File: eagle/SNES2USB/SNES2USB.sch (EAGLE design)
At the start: 46 parts, among them J1 AVR_SPI_PRG_6PTH, Y1 12-20MHz

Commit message: beta of the SNES2USB PCB
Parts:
- removed JP1, JP2: M021X02_NO_SILK, SparkFun-Connectors:M021X02_NO_SILK
- removed JP3, JP4: M161X16_NO_SILK, SparkFun-Connectors:M161X16_NO_SILK
- removed JP_ID: TEST-POINT3X5, SparkFun-Passives:TEST-POINT3X5
- removed PORTB328: (no value), SparkFun-Connectors:M081X08
- removed RAIL+, RAIL-: M17NOSILK, SparkFun-Connectors:M17NOSILK
- removed U$2, U$3, U$4, U$5, U$6: M191X19_NO_SILK, SparkFun-Connectors:M191X19_NO_SILK
- added J10, J7, J8, J9: (no value), SparkFun-Connectors:CONN_041X04_NO_SILK
- added J2, J3, J4, J5, J6: (no value), SparkFun-Connectors:CONN_08NO_SILK_FEMALE_PTH
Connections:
- removed net B0: PORTB328.1, UC2.PB0(ICP), UC328DIP.PB0(ICP)
- removed net B1: PORTB328.2, UC2.PB1(OC1A), UC328DIP.PB1(OC1A)
- removed net B2: PORTB328.3, UC2.PB2(SS/OC1B), UC328DIP.PB2(SS/OC1B)
- net B6: no longer PORTB328.7
- net B7: no longer PORTB328.8
- net GND: no longer JP2.1, JP2.2, RAIL-.1, RAIL-.10, RAIL-.11, RAIL-.12, RAIL-.13, RAIL-.14, RAIL-.15, RAIL-.16, RAIL-.17, RAIL-.2, RAIL-.3, RAIL-.4, RAIL-.5, RAIL-.6, RAIL-.7, RAIL-.8, RAIL-.9
- net MISO: no longer PORTB328.5
- net MOSI: no longer PORTB328.4
- net N$1: no longer JP_ID.1
- net SCK: no longer PORTB328.6
- net VCC: no longer JP1.1, JP1.2, RAIL+.1, RAIL+.10, RAIL+.11, RAIL+.12, RAIL+.13, RAIL+.14, RAIL+.15, RAIL+.16, RAIL+.17, RAIL+.2, RAIL+.3, RAIL+.4, RAIL+.5, RAIL+.6, RAIL+.7, RAIL+.8, RAIL+.9

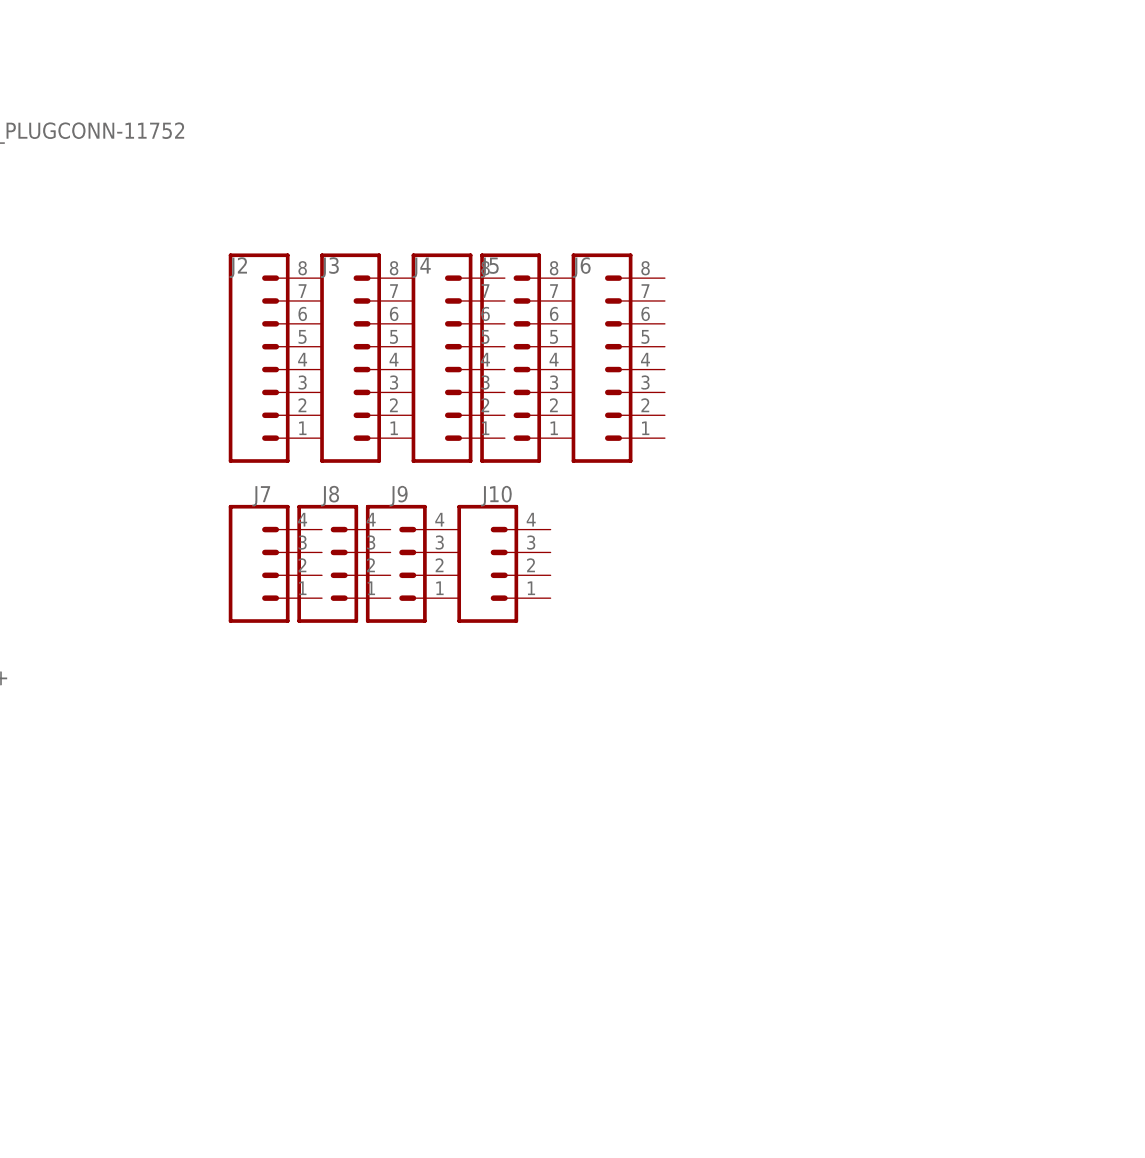
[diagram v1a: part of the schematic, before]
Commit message: SNES2USB nearly ready to be released, todo change for alternate layout of SNES pad
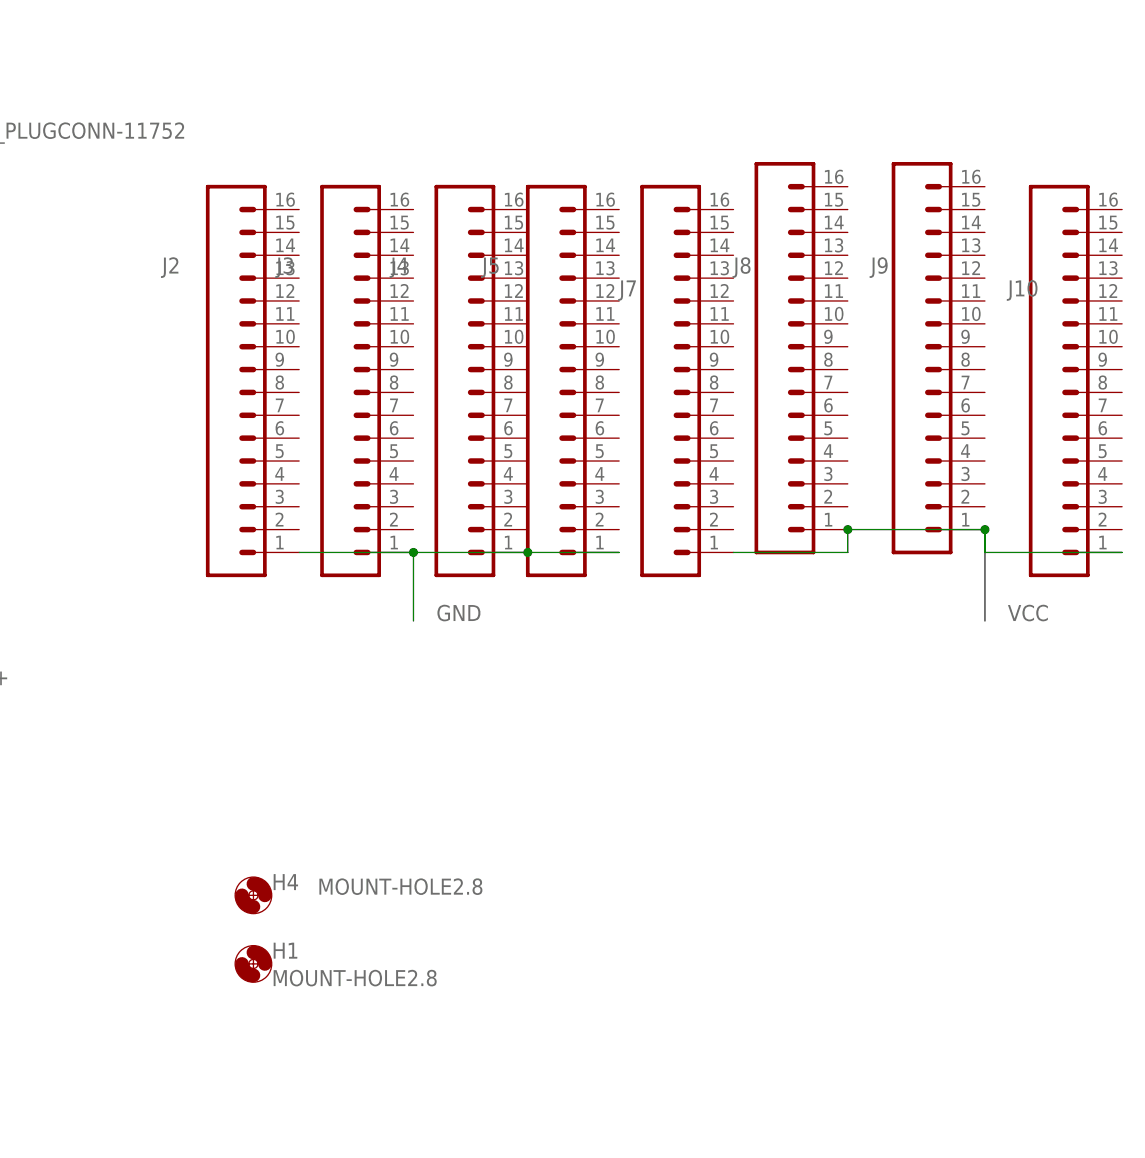
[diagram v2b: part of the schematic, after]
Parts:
- removed J6: (no value), SparkFun-Connectors:CONN_08NO_SILK_FEMALE_PTH
- added H1, H4: MOUNT-HOLE2.8, holes:MOUNT-HOLE2.8
- J10, J7, J8, J9: device SparkFun-Connectors:CONN_041X04_NO_SILK -> SparkFun-Connectors:CONN_161X16_NO_SILK
- J2, J3, J4, J5: device SparkFun-Connectors:CONN_08NO_SILK_FEMALE_PTH -> SparkFun-Connectors:CONN_161X16_NO_SILK
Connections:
- net GND: now also J2.1, J3.1, J4.1, J5.1
- net VCC: now also J10.1, J7.1, J8.1, J9.1
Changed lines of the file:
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@@
 <part name="JLATCH" library="SparkFun-Connectors" library_urn="urn:adsk.eagle:library:513" deviceset="CONN_01" device="PTH_NO_SILK_YES_STOP" package3d_urn="urn:adsk.eagle:package:38041/1"/>
 <part name="JCLK" library="SparkFun-Connectors" library_urn="urn:adsk.eagle:library:513" deviceset="CONN_01" device="PTH_NO_SILK_YES_STOP" package3d_urn="urn:adsk.eagle:package:38041/1"/>
-<part name="J2" library="SparkFun-Connectors" library_urn="urn:adsk.eagle:library:513" deviceset="CONN_08" device="NO_SILK_FEMALE_PTH" package3d_urn="urn:adsk.eagle:package:38149/1"/>
-<part name="J3" library="SparkFun-Connectors" library_urn="urn:adsk.eagle:library:513" deviceset="CONN_08" device="NO_SILK_FEMALE_PTH" package3d_urn="urn:adsk.eagle:package:38149/1"/>
-<part name="J4" library="SparkFun-Connectors" library_urn="urn:adsk.eagle:library:513" deviceset="CONN_08" device="NO_SILK_FEMALE_PTH" package3d_urn="urn:adsk.eagle:package:38149/1"/>
-<part name="J5" library="SparkFun-Connectors" library_urn="urn:adsk.eagle:library:513" deviceset="CONN_08" device="NO_SILK_FEMALE_PTH" package3d_urn="urn:adsk.eagle:package:38149/1"/>
-<part name="J6" library="SparkFun-Connectors" library_urn="urn:adsk.eagle:library:513" deviceset="CONN_08" device="NO_SILK_FEMALE_PTH" package3d_urn="urn:adsk.eagle:package:38149/1"/>
-<part name="J7" library="SparkFun-Connectors" library_urn="urn:adsk.eagle:library:513" deviceset="CONN_04" device="1X04_NO_SILK" package3d_urn="urn:adsk.eagle:package:38094/1"/>
-<part name="J8" library="SparkFun-Connectors" library_urn="urn:adsk.eagle:library:513" deviceset="CONN_04" device="1X04_NO_SILK" package3d_urn="urn:adsk.eagle:package:38094/1"/>
-<part name="J9" library="SparkFun-Connectors" library_urn="urn:adsk.eagle:library:513" deviceset="CONN_04" device="1X04_NO_SILK" package3d_urn="urn:adsk.eagle:package:38094/1"/>
-<part name="J10" library="SparkFun-Connectors" library_urn="urn:adsk.eagle:library:513" deviceset="CONN_04" device="1X04_NO_SILK" package3d_urn="urn:adsk.eagle:package:38094/1"/>
+<part name="J2" library="SparkFun-Connectors" library_urn="urn:adsk.eagle:library:513" deviceset="CONN_16" device="1X16_NO_SILK" package3d_urn="urn:adsk.eagle:package:38249/1"/>
+<part name="J3" library="SparkFun-Connectors" library_urn="urn:adsk.eagle:library:513" deviceset="CONN_16" device="1X16_NO_SILK" package3d_urn="urn:adsk.eagle:package:38249/1"/>
+<part name="J4" library="SparkFun-Connectors" library_urn="urn:adsk.eagle:library:513" deviceset="CONN_16" device="1X16_NO_SILK" package3d_urn="urn:adsk.eagle:package:38249/1"/>
+<part name="J5" library="SparkFun-Connectors" library_urn="urn:adsk.eagle:library:513" deviceset="CONN_16" device="1X16_NO_SILK" package3d_urn="urn:adsk.eagle:package:38249/1"/>
+<part name="J7" library="SparkFun-Connectors" library_urn="urn:adsk.eagle:library:513" deviceset="CONN_16" device="1X16_NO_SILK" package3d_urn="urn:adsk.eagle:package:38249/1"/>
+<part name="J8" library="SparkFun-Connectors" library_urn="urn:adsk.eagle:library:513" deviceset="CONN_16" device="1X16_NO_SILK" package3d_urn="urn:adsk.eagle:package:38249/1"/>
+<part name="J9" library="SparkFun-Connectors" library_urn="urn:adsk.eagle:library:513" deviceset="CONN_16" device="1X16_NO_SILK" package3d_urn="urn:adsk.eagle:package:38249/1"/>
+<part name="J10" library="SparkFun-Connectors" library_urn="urn:adsk.eagle:library:513" deviceset="CONN_16" device="1X16_NO_SILK" package3d_urn="urn:adsk.eagle:package:38249/1"/>
+<part name="H1" library="holes" library_urn="urn:adsk.eagle:library:237" deviceset="MOUNT-HOLE" device="2.8" package3d_urn="urn:adsk.eagle:package:14271/1"/>
+<part name="H4" library="holes" library_urn="urn:adsk.eagle:library:237" deviceset="MOUNT-HOLE" device="2.8" package3d_urn="urn:adsk.eagle:package:14271/1"/>
 </parts>
 <sheets>
@@
 <attribute name="NAME" x="127.508" y="-50.8" size="1.778" layer="95" font="vector" rot="R270"/>
 </instance>
-<instance part="J2" gate="G$1" x="129.54" y="83.82" smashed="yes">
-<attribute name="VALUE" x="124.46" y="73.914" size="1.778" layer="96" font="vector"/>
-<attribute name="NAME" x="124.46" y="94.488" size="1.778" layer="95" font="vector"/>
-</instance>
-<instance part="J3" gate="G$1" x="139.7" y="83.82" smashed="yes">
-<attribute name="VALUE" x="134.62" y="73.914" size="1.778" layer="96" font="vector"/>
-<attribute name="NAME" x="134.62" y="94.488" size="1.778" layer="95" font="vector"/>
-</instance>
-<instance part="J4" gate="G$1" x="149.86" y="83.82" smashed="yes">
-<attribute name="VALUE" x="144.78" y="73.914" size="1.778" layer="96" font="vector"/>
-<attribute name="NAME" x="144.78" y="94.488" size="1.778" layer="95" font="vector"/>
+<instance part="J2" gate="G$1" x="121.92" y="83.82" smashed="yes">
+<attribute name="VALUE" x="116.84" y="73.914" size="1.778" layer="96" font="vector"/>
+<attribute name="NAME" x="116.84" y="94.488" size="1.778" layer="95" font="vector"/>
+</instance>
+<instance part="J3" gate="G$1" x="134.62" y="83.82" smashed="yes">
+<attribute name="VALUE" x="129.54" y="73.914" size="1.778" layer="96" font="vector"/>
+<attribute name="NAME" x="129.54" y="94.488" size="1.778" layer="95" font="vector"/>
+</instance>
+<instance part="J4" gate="G$1" x="147.32" y="83.82" smashed="yes">
+<attribute name="VALUE" x="142.24" y="73.914" size="1.778" layer="96" font="vector"/>
+<attribute name="NAME" x="142.24" y="94.488" size="1.778" layer="95" font="vector"/>
 </instance>
 <instance part="J5" gate="G$1" x="157.48" y="83.82" smashed="yes">
@@
 <attribute name="NAME" x="152.4" y="94.488" size="1.778" layer="95" font="vector"/>
 </instance>
-<instance part="J6" gate="G$1" x="167.64" y="83.82" smashed="yes">
-<attribute name="VALUE" x="162.56" y="73.914" size="1.778" layer="96" font="vector"/>
-<attribute name="NAME" x="162.56" y="94.488" size="1.778" layer="95" font="vector"/>
-</instance>
-<instance part="J7" gate="G$1" x="129.54" y="60.96" smashed="yes">
-<attribute name="VALUE" x="127" y="51.054" size="1.778" layer="96" font="vector"/>
-<attribute name="NAME" x="127" y="69.088" size="1.778" layer="95" font="vector"/>
-</instance>
-<instance part="J8" gate="G$1" x="137.16" y="60.96" smashed="yes">
-<attribute name="VALUE" x="134.62" y="51.054" size="1.778" layer="96" font="vector"/>
-<attribute name="NAME" x="134.62" y="69.088" size="1.778" layer="95" font="vector"/>
-</instance>
-<instance part="J9" gate="G$1" x="144.78" y="60.96" smashed="yes">
-<attribute name="VALUE" x="142.24" y="51.054" size="1.778" layer="96" font="vector"/>
-<attribute name="NAME" x="142.24" y="69.088" size="1.778" layer="95" font="vector"/>
-</instance>
-<instance part="J10" gate="G$1" x="154.94" y="60.96" smashed="yes">
-<attribute name="VALUE" x="152.4" y="51.054" size="1.778" layer="96" font="vector"/>
-<attribute name="NAME" x="152.4" y="69.088" size="1.778" layer="95" font="vector"/>
+<instance part="J7" gate="G$1" x="170.18" y="83.82" smashed="yes">
+<attribute name="VALUE" x="167.64" y="73.914" size="1.778" layer="96" font="vector"/>
+<attribute name="NAME" x="167.64" y="91.948" size="1.778" layer="95" font="vector"/>
+</instance>
+<instance part="J8" gate="G$1" x="182.88" y="86.36" smashed="yes">
+<attribute name="VALUE" x="180.34" y="76.454" size="1.778" layer="96" font="vector"/>
+<attribute name="NAME" x="180.34" y="94.488" size="1.778" layer="95" font="vector"/>
+</instance>
+<instance part="J9" gate="G$1" x="198.12" y="86.36" smashed="yes">
+<attribute name="VALUE" x="195.58" y="76.454" size="1.778" layer="96" font="vector"/>
+<attribute name="NAME" x="195.58" y="94.488" size="1.778" layer="95" font="vector"/>
+</instance>
+<instance part="J10" gate="G$1" x="213.36" y="83.82" smashed="yes">
+<attribute name="VALUE" x="210.82" y="73.914" size="1.778" layer="96" font="vector"/>
+<attribute name="NAME" x="210.82" y="91.948" size="1.778" layer="95" font="vector"/>
+</instance>
+<instance part="H1" gate="G$1" x="127" y="17.78" smashed="yes">
+<attribute name="NAME" x="129.032" y="18.3642" size="1.778" layer="95"/>
+<attribute name="VALUE" x="129.032" y="15.3162" size="1.778" layer="96"/>
+</instance>
+<instance part="H4" gate="G$1" x="127" y="25.4" smashed="yes">
+<attribute name="NAME" x="129.032" y="25.9842" size="1.778" layer="95"/>
+<attribute name="VALUE" x="134.112" y="25.4762" size="1.778" layer="96"/>
 </instance>
 </instances>
@@
 <label x="76.2" y="-68.58" size="1.778" layer="95"/>
 </segment>
+<segment>
+<pinref part="J7" gate="G$1" pin="1"/>
+<wire x1="180.34" y1="63.5" x2="193.04" y2="63.5" width="0.1524" layer="91"/>
+<pinref part="J8" gate="G$1" pin="1"/>
+<wire x1="193.04" y1="63.5" x2="193.04" y2="66.04" width="0.1524" layer="91"/>
+<pinref part="J9" gate="G$1" pin="1"/>
+<wire x1="193.04" y1="66.04" x2="208.28" y2="66.04" width="0.1524" layer="91"/>
+<junction x="193.04" y="66.04"/>
+<wire x1="208.28" y1="66.04" x2="208.28" y2="63.5" width="0.1524" layer="91"/>
+<junction x="208.28" y="66.04"/>
+<pinref part="J10" gate="G$1" pin="1"/>
+<wire x1="208.28" y1="63.5" x2="223.52" y2="63.5" width="0.1524" layer="91"/>
+<wire x1="208.28" y1="66.04" x2="208.28" y2="55.88" width="0.1524" layer="91"/>
+<label x="210.82" y="55.88" size="1.778" layer="95"/>
+</segment>
 </net>
 <net name="GND" class="0">
@@
 <label x="76.2" y="-30.48" size="1.778" layer="95"/>
 </segment>
+<segment>
+<pinref part="J2" gate="G$1" pin="1"/>
+<pinref part="J3" gate="G$1" pin="1"/>
+<wire x1="132.08" y1="63.5" x2="144.78" y2="63.5" width="0.1524" layer="91"/>
+<pinref part="J4" gate="G$1" pin="1"/>
+<wire x1="144.78" y1="63.5" x2="157.48" y2="63.5" width="0.1524" layer="91"/>
+<junction x="144.78" y="63.5"/>
+<pinref part="J5" gate="G$1" pin="1"/>
+<wire x1="157.48" y1="63.5" x2="167.64" y2="63.5" width="0.1524" layer="91"/>
+<junction x="157.48" y="63.5"/>
+<wire x1="144.78" y1="63.5" x2="144.78" y2="55.88" width="0.1524" layer="91"/>
+<label x="147.32" y="55.88" size="1.778" layer="95"/>
+</segment>
 </net>
